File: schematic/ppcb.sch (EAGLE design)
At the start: 13 parts, among them U1 ATTINY*5, U2 LM211N

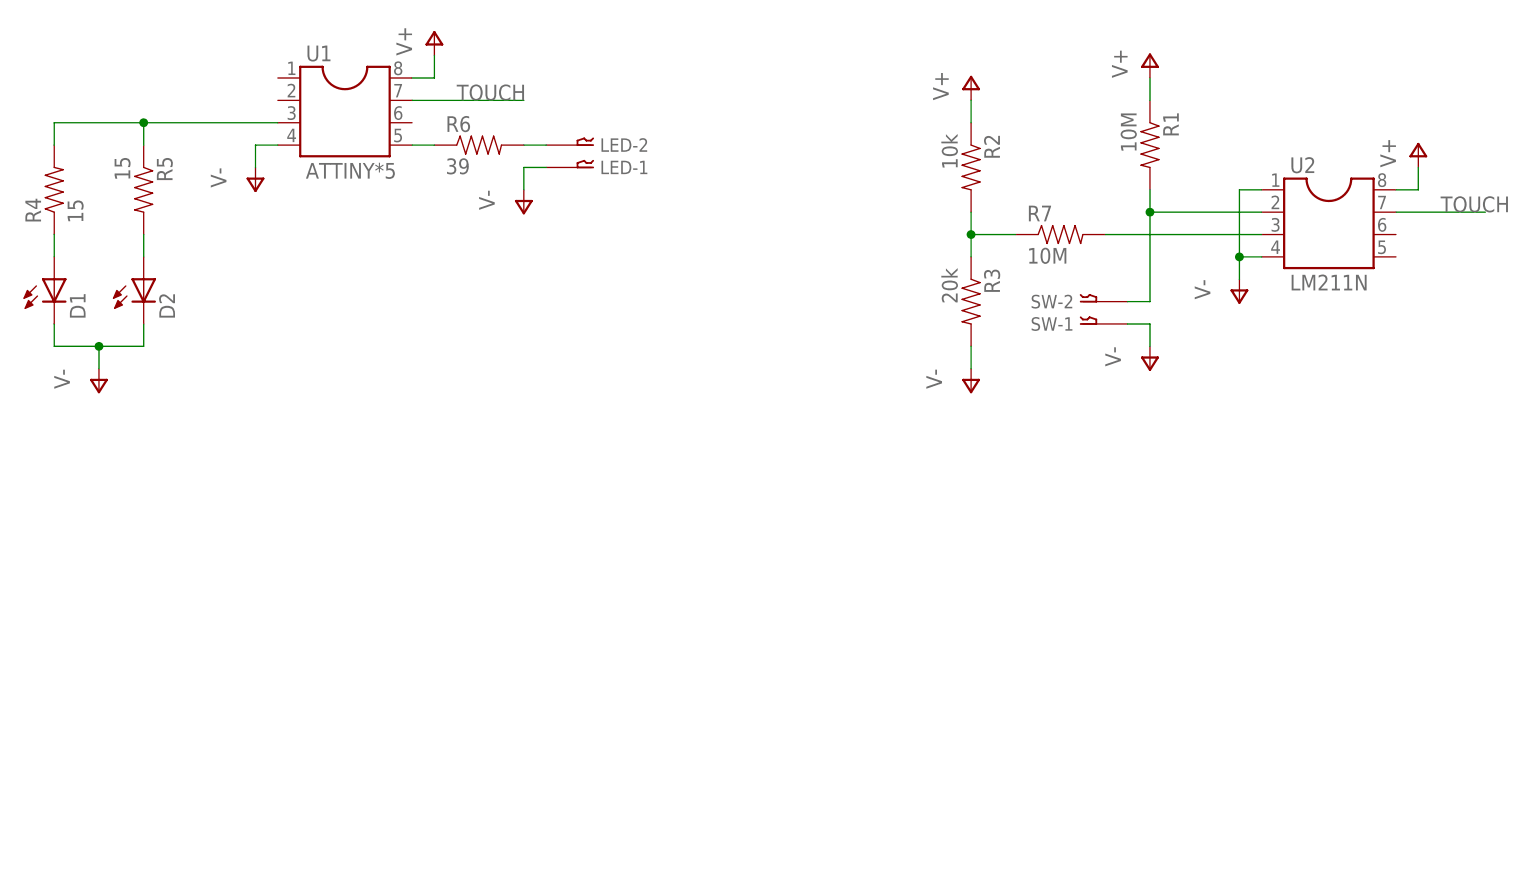
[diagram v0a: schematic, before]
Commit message: Updated PCB to remove external analog comparator and make use of Timer/Counter-1 instead of Timer/Counter-0
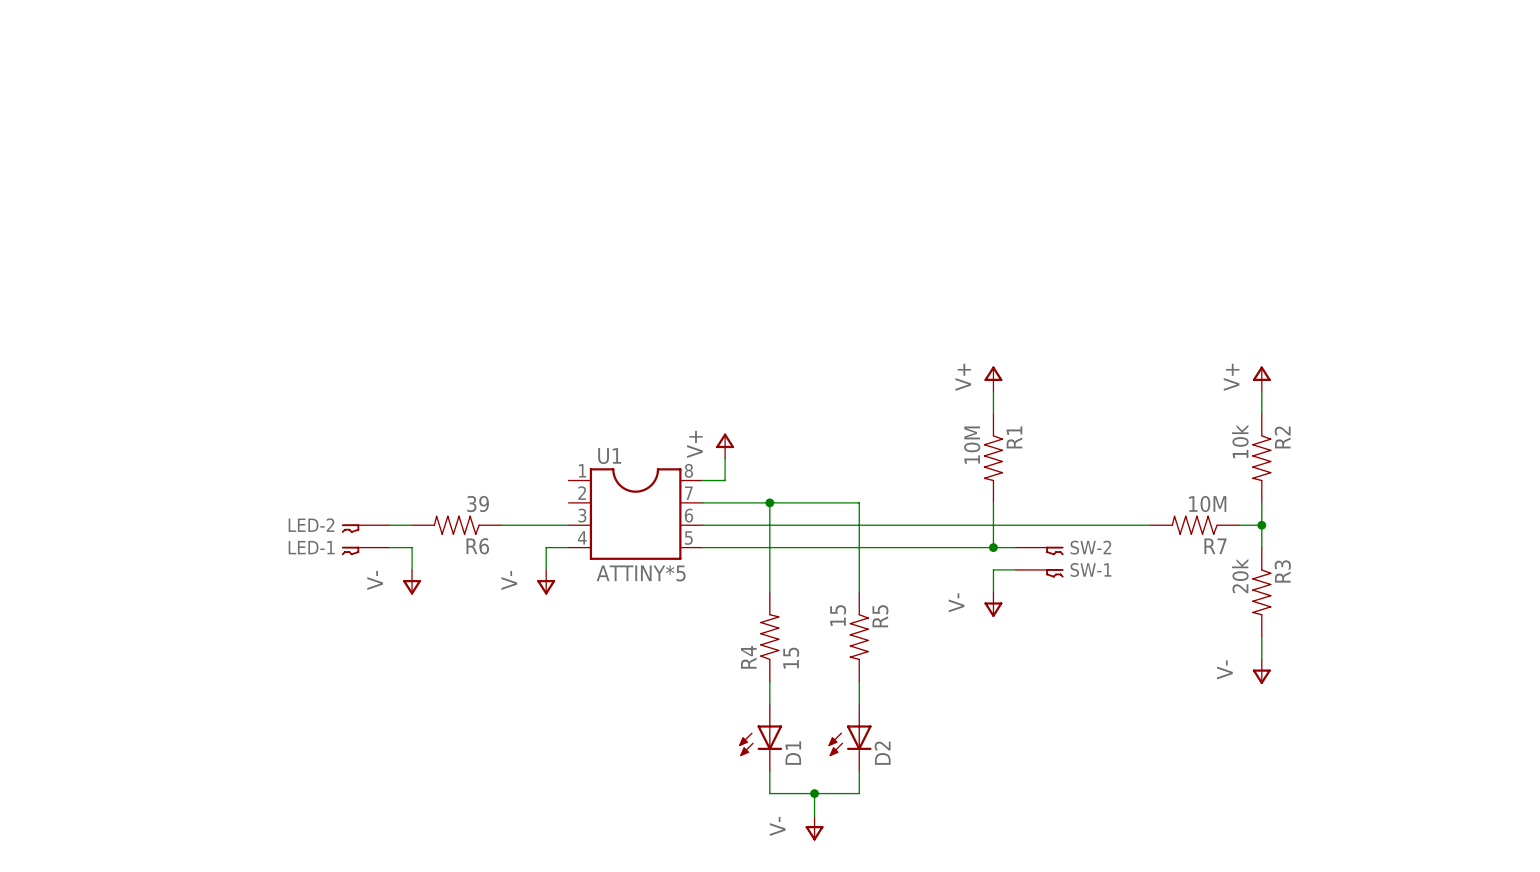
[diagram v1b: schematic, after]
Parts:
- removed U2: LM211N, ic-package:DIL8S
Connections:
- removed net TOUCH: U1.7, U2.7
- net N$1: now also U1.5; no longer U2.2
- net N$2: now also R7.2, U1.6; no longer R6.1, U1.5
- net N$7: now also R6.1, U1.3; no longer R7.2, U2.3
- net N$9: now also U1.7; no longer U1.3
- net V+: no longer U2.8
- net V-: no longer U2.1, U2.4
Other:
- moved on the sheet: D1, D2, LED-1, LED-2, R1, R2, R3, R4, R5, R6, R7, SW-1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
